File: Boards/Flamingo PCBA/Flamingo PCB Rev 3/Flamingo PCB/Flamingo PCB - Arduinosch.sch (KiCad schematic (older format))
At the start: 6 parts

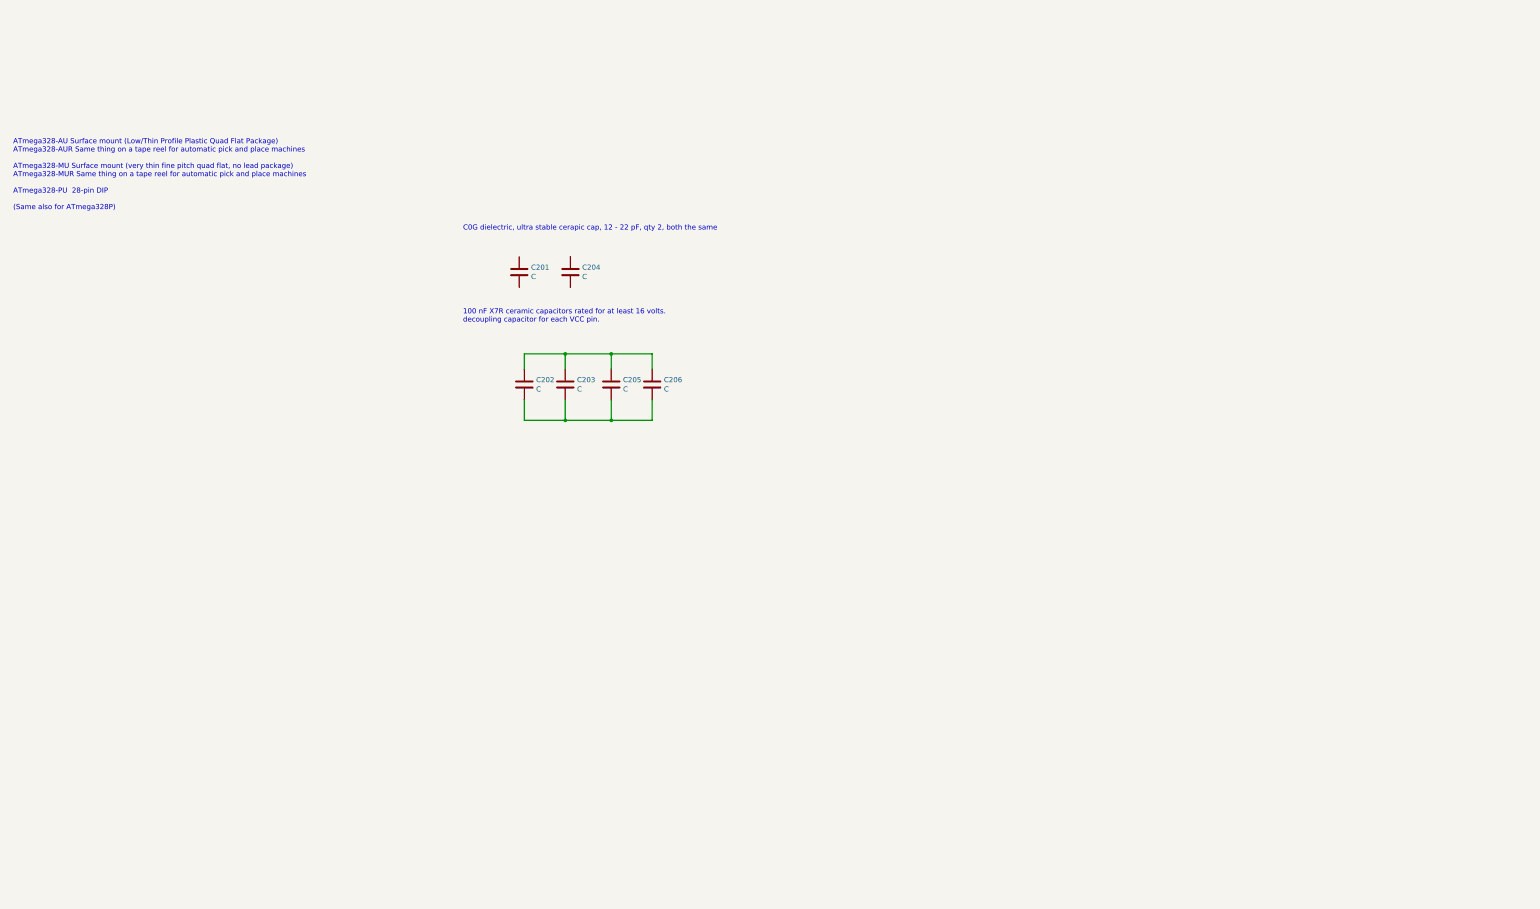
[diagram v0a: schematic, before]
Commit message: Worked on Power board mainly.
Still have to resolve the power sharing.
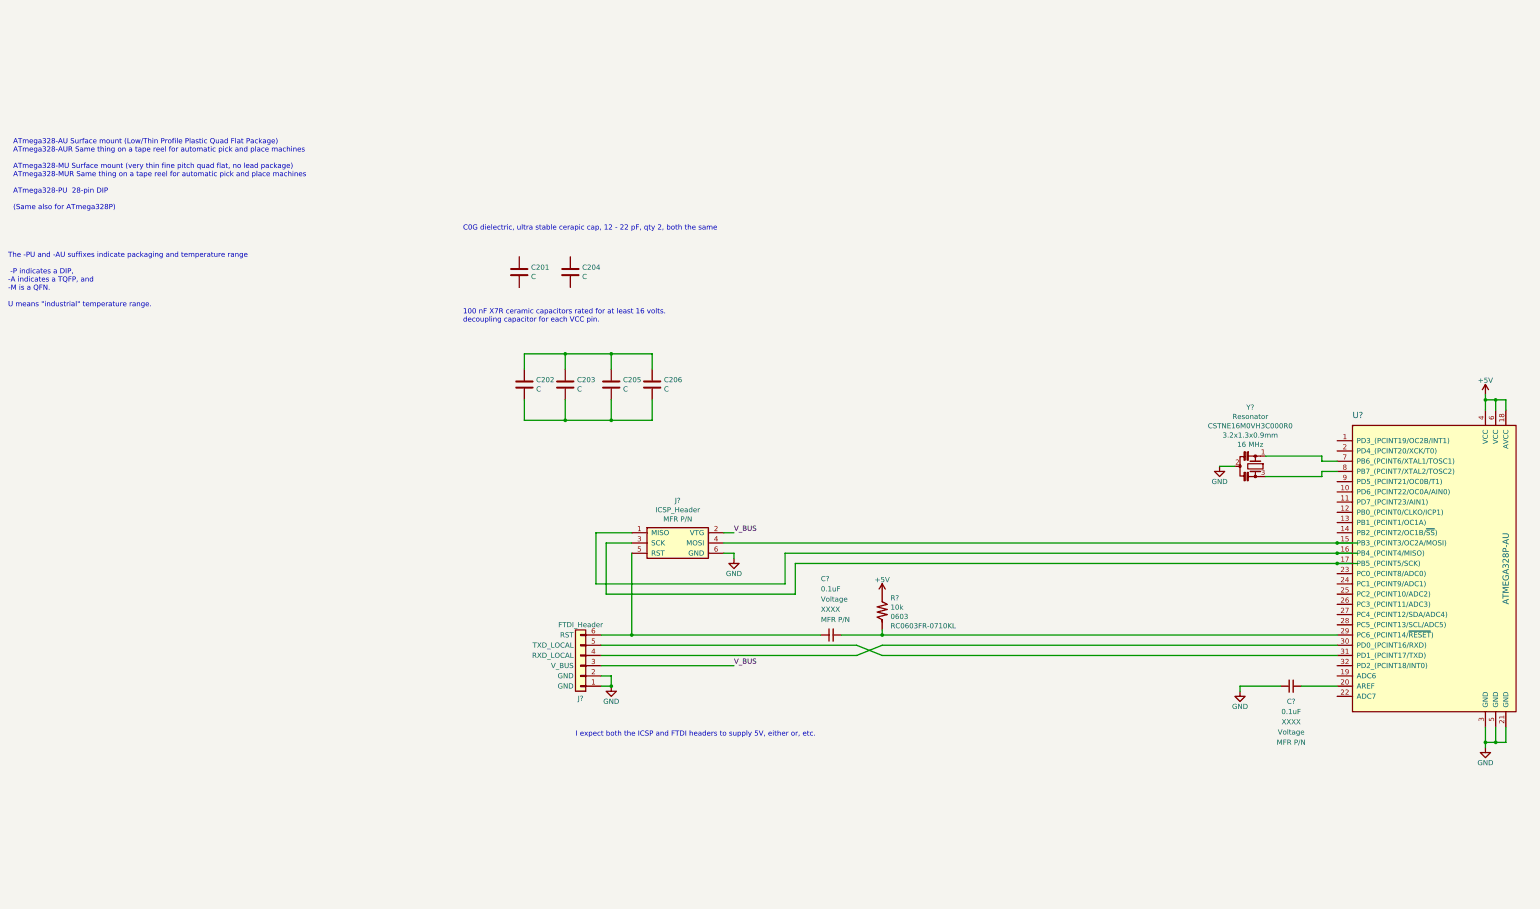
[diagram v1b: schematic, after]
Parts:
- added C? (x2): 0.1uF, symbol MyCapacitors:C_Small_horizontal
- added J?: FTDI_Header, symbol MyConnectors:FTDI_Header
- added J?: ICSP_Header, symbol MyConnectors:ISP_Header
- added R?: 10k, Resistors_SMD:R_0603_HandSoldering, symbol MyResistors:R_vert
- added U?: ATMEGA328P-AU, digikey-footprints:TQFP-32_7x7mm, symbol MyICs:ATMEGA328P-AU
- added Y?: Resonator, symbol MyCrystals:Resonator_Small_vert
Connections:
- net labels added: +5V, GND, V_BUS
- wire segments 14 -> 69
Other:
- note added: "I expect both the ICSP and FTDI headers to supply 5V, either or, etc."
- note added: "The -PU and -AU suffixes indicate packaging and temperature range\n\n -P indicates a DIP, \n-A indicates a TQFP, and \n-M is a QFN. \n\nU means "industrial" temperature range."

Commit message: NOSTUFF 5V LDO bc not needed. Added Sch diode on 5v LDO.
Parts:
- gave numbers to parts that had none: 7
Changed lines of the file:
@@
 The -PU and -AU suffixes indicate packaging and temperature range\n\n -P indicates a DIP, \n-A indicates a TQFP, and \n-M is a QFN.  \n\nU means "industrial" temperature range.
 $Comp
-L MyConnectors:FTDI_Header J?
+L MyConnectors:FTDI_Header J201
 U 1 1 5F844162
 P 1850 5400
-F 0 "J?" H 1850 5750 50  0000 C TNN
+F 0 "J201" H 1850 5750 50  0000 C TNN
 F 1 "FTDI_Header" H 1850 5000 50  0000 C CNN
 F 2 "" H 1850 5400 50  0001 C CNN
@@
 $EndComp
 $Comp
-L MyICs:ATMEGA328P-AU U?
+L MyICs:ATMEGA328P-AU U201
 U 1 1 5F846AEA
 P 10700 4500
-F 0 "U?" H 9400 6050 60  0000 L CNN
+F 0 "U201" H 9400 6050 60  0000 L CNN
 F 1 "ATMEGA328P-AU" V 10900 4550 60  0000 C CNN
 F 2 "digikey-footprints:TQFP-32_7x7mm" H 11250 4700 60  0001 L CNN
@@
 	2150 5500 2150 5600
 $Comp
-L power:GND #PWR?
+L power:GND #PWR0201
 U 1 1 5F84DF41
 P 2150 5600
-F 0 "#PWR?" H 2150 5350 50  0001 C CNN
+F 0 "#PWR0201" H 2150 5350 50  0001 C CNN
 F 1 "GND" H 2150 5450 50  0000 C CNN
 F 2 "" H 2150 5600 50  0001 C CNN
@@
 Connection ~ 2150 5600
 $Comp
-L power:+5V #PWR?
+L power:+5V #PWR0203
 U 1 1 5F84F6BB
 P 4800 4700
-F 0 "#PWR?" H 4800 4550 50  0001 C CNN
+F 0 "#PWR0203" H 4800 4550 50  0001 C CNN
 F 1 "+5V" H 4800 4840 50  0000 C CNN
 F 2 "" H 4800 4700 50  0001 C CNN
@@
 P 4800 4850
 AR Path="/5F780D75/5F8530A4" Ref="R?"  Part="1"
-AR Path="/5F780A01/5F8530A4" Ref="R?"  Part="1"
-F 0 "R?" H 4881 4962 50  0000 L CNN
+AR Path="/5F780A01/5F8530A4" Ref="R201"  Part="1"
+F 0 "R201" H 4881 4962 50  0000 L CNN
 F 1 "10k" H 4881 4871 50  0000 L CNN
 F 2 "Resistors_SMD:R_0603_HandSoldering" V 4855 4800 50  0001 C CNN
@@
 $EndComp
 $Comp
-L MyCapacitors:C_Small_horizontal C?
+L MyCapacitors:C_Small_horizontal C207
 U 1 1 5F85B8E0
 P 4400 5050
-F 0 "C?" H 4200 5550 50  0000 L CNN
+F 0 "C207" H 4200 5550 50  0000 L CNN
 F 1 "0.1uF" H 4200 5450 50  0000 L CNN
 F 2 "" V 4275 5000 50  0001 L CNN
@@
 $EndComp
 $Comp
-L power:GND #PWR?
+L power:GND #PWR0207
 U 1 1 5F861345
 P 10700 6200
-F 0 "#PWR?" H 10700 5950 50  0001 C CNN
+F 0 "#PWR0207" H 10700 5950 50  0001 C CNN
 F 1 "GND" H 10700 6050 50  0000 C CNN
 F 2 "" H 10700 6200 50  0001 C CNN
@@
 	4800 5200 4550 5300
 $Comp
-L power:+5V #PWR?
+L power:+5V #PWR0206
 U 1 1 5F869CB1
 P 10700 2750
-F 0 "#PWR?" H 10700 2600 50  0001 C CNN
+F 0 "#PWR0206" H 10700 2600 50  0001 C CNN
 F 1 "+5V" H 10700 2890 50  0000 C CNN
 F 2 "" H 10700 2750 50  0001 C CNN
@@
 	9100 3400 9250 3400
 $Comp
-L power:GND #PWR?
+L power:GND #PWR0204
 U 1 1 5F8980D8
 P 8100 3450
-F 0 "#PWR?" H 8100 3200 50  0001 C CNN
+F 0 "#PWR0204" H 8100 3200 50  0001 C CNN
 F 1 "GND" H 8100 3300 50  0000 C CNN
 F 2 "" H 8100 3450 50  0001 C CNN
@@
 	8100 3450 8250 3450
 $Comp
-L MyCrystals:Resonator_Small_vert Y?
+L MyCrystals:Resonator_Small_vert Y201
 U 1 1 5F8A8BD5
 P 8450 3450
-F 0 "Y?" V 7873 3400 50  0000 C CNN
+F 0 "Y201" V 7873 3400 50  0000 C CNN
 F 1 "Resonator" V 7964 3400 50  0000 C CNN
 F 2 "" H 8425 3450 50  0001 C CNN
@@
 Connection ~ 10800 2800
 $Comp
-L MyCapacitors:C_Small_horizontal C?
+L MyCapacitors:C_Small_horizontal C208
 U 1 1 5F8AF43A
 P 8900 5550
-F 0 "C?" H 8800 5350 50  0000 C CNN
+F 0 "C208" H 8800 5350 50  0000 C CNN
 F 1 "0.1uF" H 8800 5250 50  0000 C CNN
 F 2 "" V 8775 5500 50  0001 L CNN
@@
 	8900 5600 9250 5600
 $Comp
-L power:GND #PWR?
+L power:GND #PWR0205
 U 1 1 5F8B38E2
 P 8300 5650
-F 0 "#PWR?" H 8300 5400 50  0001 C CNN
+F 0 "#PWR0205" H 8300 5400 50  0001 C CNN
 F 1 "GND" H 8300 5500 50  0000 C CNN
 F 2 "" H 8300 5650 50  0001 C CNN
@@
 	3250 4100 3350 4100
 $Comp
-L power:GND #PWR?
+L power:GND #PWR0202
 U 1 1 5F8CB74A
 P 3350 4350
-F 0 "#PWR?" H 3350 4100 50  0001 C CNN
+F 0 "#PWR0202" H 3350 4100 50  0001 C CNN
 F 1 "GND" H 3350 4200 50  0000 C CNN
 F 2 "" H 3350 4350 50  0001 C CNN
@@
 $EndComp
 $Comp
-L MyConnectors:ISP_Header J?
+L MyConnectors:ISP_Header J202
 U 1 1 5F8B5E79
 P 2350 4100
-F 0 "J?" H 2800 4415 50  0000 C CNN
+F 0 "J202" H 2800 4415 50  0000 C CNN
 F 1 "ICSP_Header" H 2800 4324 50  0000 C CNN
 F 2 "" H 2600 3750 50  0001 L CNN

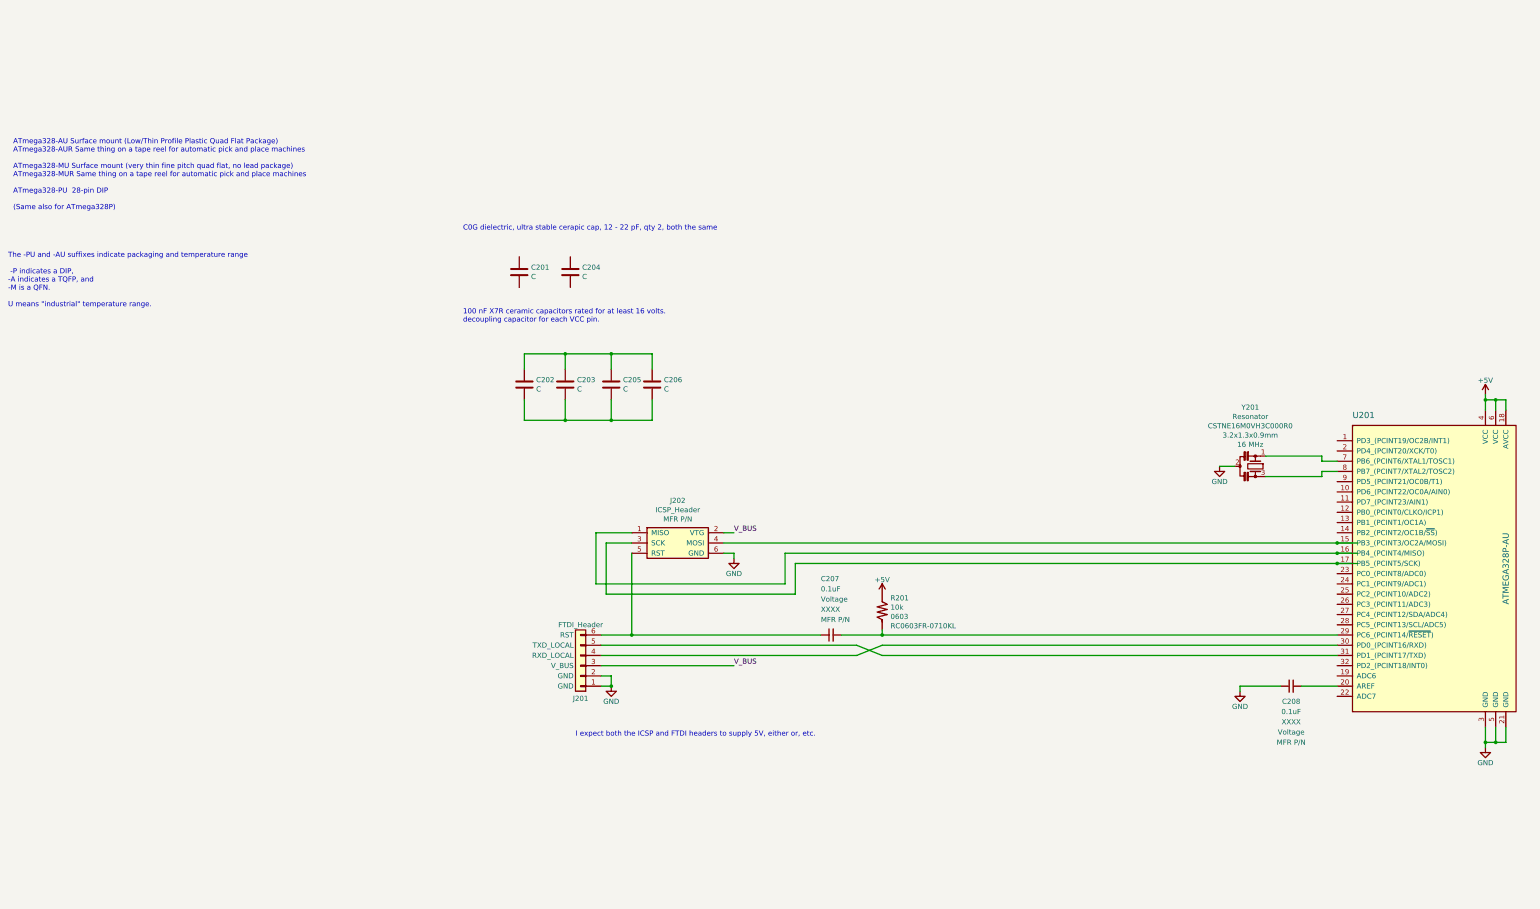
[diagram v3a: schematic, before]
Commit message: More work on Arduino schematic, created button board schematic
Button board schematic should probably be a separate project
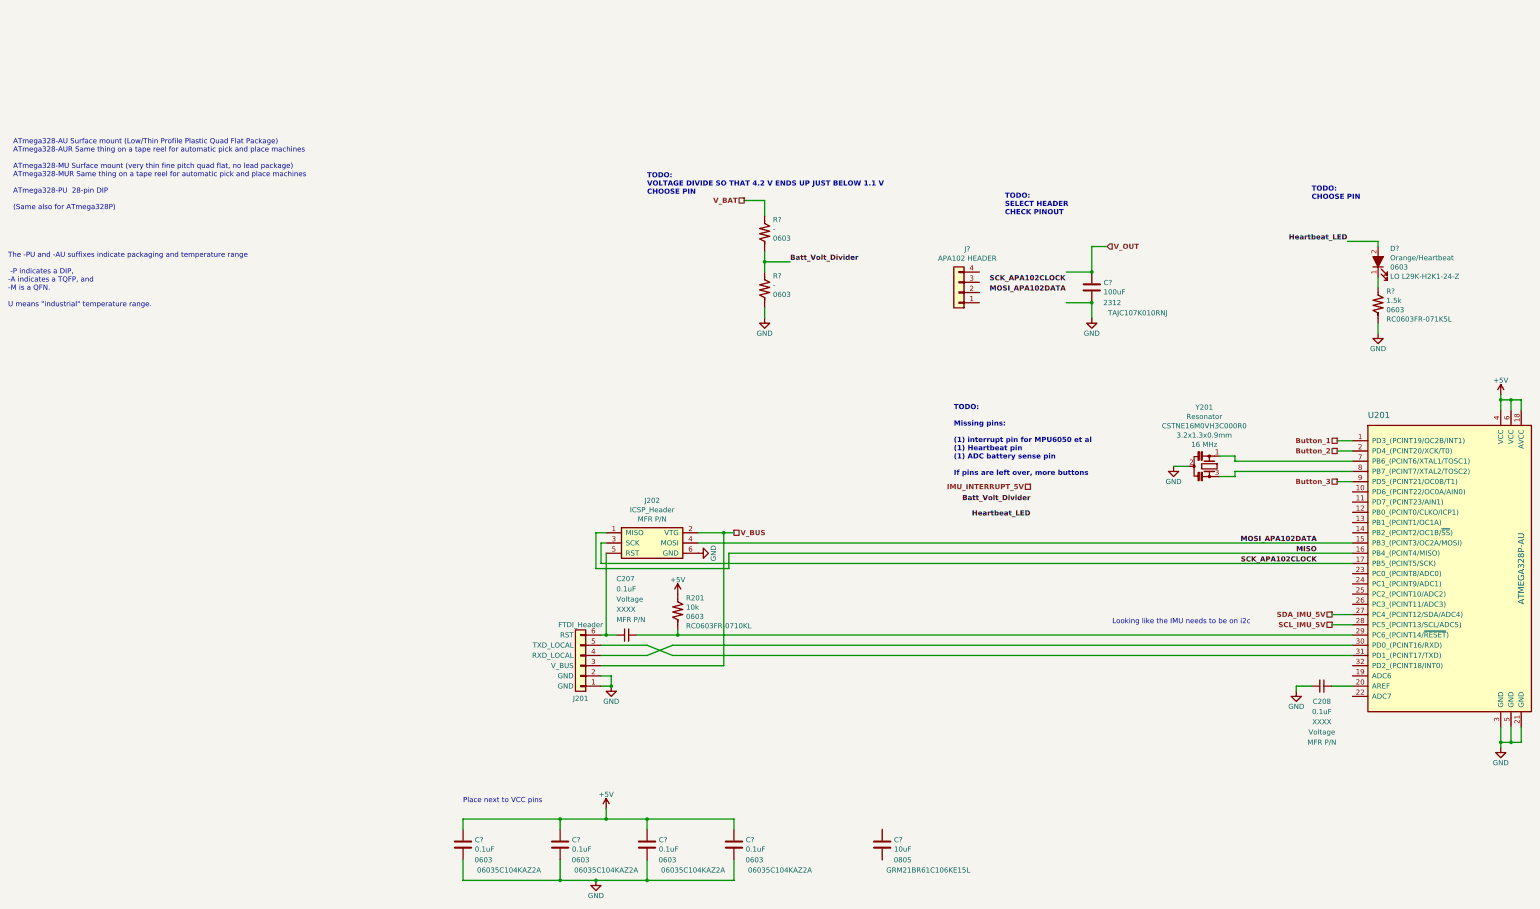
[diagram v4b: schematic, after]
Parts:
- removed C201, C202, C203, C204, C205, C206: C, symbol Device:C
- added C?: 10uF, Capacitors_SMD:C_0805_HandSoldering, symbol Device:C
- added C?: 100uF, Capacitors_Tantalum_SMD:CP_Tantalum_Case-C_EIA-6032-28_Reflow, symbol Device:C
- added C? (x4): 0.1uF, Capacitors_SMD:C_0603_HandSoldering, symbol Device:C
- added D?: Orange/Heartbeat, LEDs:LED_0603_HandSoldering, symbol MyLEDs:LED_ALT_vert
- added J?: APA102 HEADER, symbol Connector_Generic:Conn_01x04
- added R?: 1.5k, Resistors_SMD:R_0603_HandSoldering, symbol MyResistors:R_vert
- added R? (x2): -, Resistors_SMD:R_0603_HandSoldering, symbol MyResistors:R_vert
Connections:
- net labels added: Batt_Volt_Divider, Button_1, Button_2, Button_3, Heartbeat_LED, IMU_INTERRUPT_5V, MISO, MOSI_APA102DATA, SCK_APA102CLOCK, SCL_IMU_5V, SDA_IMU_5V, V_BAT, V_OUT
- wire segments 69 -> 87
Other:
- note added: "Looking like the IMU needs to be on i2c"
- note added: "Place next to VCC pins"
- note added: "TODO: \nCHOOSE PIN"
- note added: "TODO: \nSELECT HEADER\nCHECK PINOUT"
- note added: "TODO: \nVOLTAGE DIVIDE SO THAT 4.2 V ENDS UP JUST BELOW 1.1 V\nCHOOSE PIN"
- note added: "TODO: \n\nMissing pins:\n\n(1) interrupt pin for MPU6050 et al\n(1) Heartbeat pin\n(1) ADC battery sense pin\n\nIf pins are left over, more buttons"
- note removed: "100 nF X7R ceramic capacitors rated for at least 16 volts. \ndecoupling capacitor for each VCC pin."
- note removed: "C0G dielectric, ultra stable cerapic cap, 12 - 22 pF, qty 2, both the same"
- note removed: "I expect both the ICSP and FTDI headers to supply 5V, either or, etc."
- moved on the sheet: C207, C208, J202, R201, U201, Y201

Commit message: More work on Arduino sheet
Added V_BUS sensing, removed V_BAT sensing bc it would be a discharge situation. Assigned some lines to pins. Added placeholders for headers.
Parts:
- added J?: Button Board Connector, symbol Connector_Generic:Conn_01x05
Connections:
- net V_BAT is gone; now on net V_OUT: R?.1
- net +5V: now also C?.1
- net Batt_Volt_Divider: now also U201.22 (ADC7)
- net Button_1: now also J?.4 (Pin_4)
- net Button_2: now also J?.3 (Pin_3)
- net Button_3: now also J?.2 (Pin_2)
- net GND: now also C?.2, J?.1 (Pin_1)
- net Heartbeat_LED: now also U201.23 (PC0_(PCINT8/ADC0))
- net IMU_INTERRUPT_5V: now also U201.32 (PD2_(PCINT18/INT0))
- net V_BUS: now also U201.24 (PC1_(PCINT9/ADC1))
- net V_OUT: now also J?.5 (Pin_5)
- net MOSI_APA102DATA renamed MOSI__APA102DATA
- net SCK_APA102CLOCK renamed SCK__APA102CLOCK
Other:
- note added: "ADXL345 2 interrupt pins i2c acc only\nICM20948 1 interrupt pin i2c/aux acc gyro mag\nMPU6050 1 interrupt pin i2c ACC GYRO\nBNO055 1 interrupt pin, 1 reset pin i2c acc gyro mag\n"
- note added: "Ideas:\n\nOne on-board button for convenience. (adds a resistor and a button)\nDIP switch (adds resistor per switch)"
- note added: "If we use V_OUT, we can sense batt voltage up to 4.2 V, \nand if USB is connected, we can use an additional digital pin to sense that line."
- note added: "Sensing USB power or not: V_BUS will be pulled to GND through 100k when there is nothing on USB.\nUse digital read to determine."
- note added: "TODO: \nSELECT CONNECTOR\nCHECK PINOUT"
- note added: "TODO: \n\nSELECT CONNECTOR FOR BUTTON BOARD CABLE.\nUSE AS MANY POSITIONS AS THERE ARE FREE PINS, \nSO THIS CAN BE AN EXTENSION HEADER"
- note added: "Vf = 1.8V, 2 mA Ityp\n5V-1.8 = 3.2V\n3.2V/1.5k = 2.1 mA"
- note removed: "Looking like the IMU needs to be on i2c"
- note removed: "TODO: \nCHOOSE PIN"
- note removed: "TODO: \nSELECT HEADER\nCHECK PINOUT"
- note removed: "TODO: \n\nMissing pins:\n\n(1) interrupt pin for MPU6050 et al\n(1) Heartbeat pin\n(1) ADC battery sense pin\n\nIf pins are left over, more buttons"
- moved on the sheet: C208, C?, D?, J?, R?
